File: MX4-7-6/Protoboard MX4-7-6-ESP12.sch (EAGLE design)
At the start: 294 parts

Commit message: Adjusted Polygon
Adjusted Polygon on all boxes. Changed length on MX-4-7-6 to fit the
box, it was 2mm to long.
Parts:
- removed PAD1, PAD119, PAD120, PAD121, PAD128, PAD129, PAD130, PAD137, PAD138, PAD139, PAD146, PAD147, PAD148, PAD151, PAD152, PAD153, PAD154, PAD155, PAD156, PAD157, PAD160, PAD161, PAD162, PAD163, PAD164, PAD165, PAD166, PAD2, PAD260, PAD261, PAD262, PAD263, PAD264, PAD265, PAD266, PAD273, PAD274, PAD275, PAD314, PAD315, PAD316, PAD317, PAD318, PAD319, PAD320, PAD332, PAD333, PAD334, PAD335, PAD336, PAD337, PAD338, PAD341, PAD342, PAD343, PAD344, PAD345, PAD346, PAD347, PAD350, PAD351, PAD352, PAD353, PAD354, PAD355, PAD356, PAD359, PAD360, PAD361, PAD362, PAD363, PAD364, PAD365, PAD368, PAD369, PAD370, PAD371, PAD372, PAD373, PAD374, PAD377, PAD378, PAD379, PAD380, PAD381, PAD382, PAD383, PAD385, PAD386, PAD387, PAD388, PAD389, PAD391, PAD392, PAD393, PAD394: (no value), wirepad:1,6/0,8
- removed X1: (no value), microbuilder:USBMICRO_20329
- added 5V, PAD104, PAD105, PAD113, PAD114, PAD3, PAD37, PAD41, PAD44, PAD48, PAD49, PAD50, PAD52, PAD53, PAD54, PAD56, PAD57, PAD58, PAD60, PAD61, PAD62, PAD64, PAD65, PAD66, PAD68, PAD69, PAD70, PAD71, PAD72, PAD73, PAD74, PAD76, PAD77, PAD78, PAD87, PAD96: (no value), wirepad:1,6/0,8
- added JP3: TX, adafruit:PINHD-1X1CB
- added JP4: RX, adafruit:PINHD-1X1CB
- added JP5: GND, adafruit:PINHD-1X1CB
- added MDL1: (no value), ESP8266-ESP12E:ESP8266-12EESP8266-ESP12E
- added MIC5502: (no value), SparkFun-PowerIC:MIC52053.3V
- added PAD47: AC, wirepad:1,6/0,8
- added PAD51: CH, wirepad:1,6/0,8
- added PAD55: 16, wirepad:1,6/0,8
- added PAD59: 14, wirepad:1,6/0,8
- added PAD63: 12, wirepad:1,6/0,8
- added PAD67: 13, wirepad:1,6/0,8
- added PAD75: CS, wirepad:1,6/0,8
- added PAD86: SI, wirepad:1,6/0,8
- added PAD95: RS, wirepad:1,6/0,8
- added X2: (no value), microbuilder:USBMICRO_20329
- PAD100: value (none) -> 5
- PAD103: value (none) -> SO
- PAD109: value (none) -> 4
- PAD111: value (none) -> 9
- PAD118: value (none) -> 0
- PAD127: value (none) -> 2
- PAD136: value (none) -> 15
- PAD145: value (none) -> SC
- PAD82: value (none) -> TX
- PAD91: value (none) -> RX
- PAD94: value (none) -> 10
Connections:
- removed net N$15: PAD151.P, PAD152.P, PAD153.P, PAD154.P, PAD155.P, PAD156.P, PAD157.P
- removed net N$16: PAD160.P, PAD161.P, PAD162.P, PAD163.P, PAD164.P, PAD165.P, PAD166.P
- removed net N$27: PAD260.P, PAD261.P, PAD262.P, PAD263.P, PAD264.P, PAD265.P, PAD266.P
- removed net N$3: PAD1.P, PAD2.P
- removed net N$33: PAD314.P, PAD315.P, PAD316.P, PAD317.P, PAD318.P, PAD319.P, PAD320.P
- removed net N$36: PAD341.P, PAD342.P, PAD343.P, PAD344.P, PAD345.P, PAD346.P, PAD347.P
- removed net N$37: PAD350.P, PAD351.P, PAD352.P, PAD353.P, PAD354.P, PAD355.P, PAD356.P
- removed net N$40: PAD377.P, PAD378.P, PAD379.P, PAD380.P, PAD381.P, PAD382.P, PAD383.P
- removed net N$41: PAD385.P, PAD386.P, PAD387.P, PAD388.P, PAD389.P
- removed net N$7: PAD79.P, PAD80.P, PAD81.P, PAD82.P, PAD83.P, PAD84.P, PAD85.P
- removed net N$8: PAD88.P, PAD89.P, PAD90.P, PAD91.P, PAD92.P, PAD93.P, PAD94.P
- new net N$26: MDL1.GPIO14, PAD59.P, PAD60.P, PAD61.P, PAD62.P
- new net N$42: MDL1.GPIO9, PAD111.P, PAD112.P, PAD113.P, PAD114.P
- new net N$50: MDL1.REST, PAD101.P, PAD102.P, PAD95.P, PAD96.P
- new net N$51: MDL1.ADC, PAD47.P, PAD48.P, PAD49.P, PAD50.P
- new net N$52: MDL1.CH_PD, PAD51.P, PAD52.P, PAD53.P, PAD54.P
- new net N$53: MDL1.GPIO16, PAD55.P, PAD56.P, PAD57.P, PAD58.P
- new net N$55: MDL1.GPIO12, PAD63.P, PAD64.P, PAD65.P, PAD66.P
- new net N$56: MDL1.GPIO13, PAD67.P, PAD68.P, PAD69.P, PAD70.P
- new net N$58: MDL1.MISO, PAD103.P, PAD104.P, PAD105.P, PAD110.P
- new net RX: JP4.1, MDL1.RXD, PAD88.P, PAD89.P, PAD90.P, PAD91.P
- new net TX: JP3.1, MDL1.TXD, PAD79.P, PAD80.P, PAD81.P, PAD82.P
- net GND: now also JP5.1, MDL1.GND, MIC5502.GND, X2.GND; no longer X1.GND
- net N$1: now also PAD3.P, PAD37.P, PAD41.P, PAD44.P; no longer PAD391.P, PAD392.P, PAD393.P, PAD394.P
- net N$10: now also MDL1.GPIO4; no longer PAD110.P, PAD111.P, PAD112.P
- net N$11: now also MDL1.GPIO0; no longer PAD119.P, PAD120.P, PAD121.P
- net N$12: now also MDL1.GPIO2; no longer PAD128.P, PAD129.P, PAD130.P
- net N$13: now also MDL1.GPIO15; no longer PAD137.P, PAD138.P, PAD139.P
- net N$14: now also MDL1.SCLK; no longer PAD146.P, PAD147.P, PAD148.P
- net N$28: no longer PAD273.P, PAD274.P, PAD275.P
- net N$29: now also PAD71.P
- net N$30: now also PAD72.P
- net N$31: now also PAD73.P
- net N$32: now also PAD74.P
- net N$35: now also MDL1.CS0, PAD75.P, PAD76.P, PAD77.P, PAD78.P; no longer PAD332.P, PAD333.P, PAD334.P, PAD335.P, PAD336.P, PAD337.P, PAD338.P
- net N$38: now also MDL1.MOSI, PAD83.P, PAD84.P, PAD85.P, PAD86.P; no longer PAD359.P, PAD360.P, PAD361.P, PAD362.P, PAD363.P, PAD364.P, PAD365.P
- net N$39: now also MDL1.GPIO10, PAD87.P, PAD92.P, PAD93.P, PAD94.P; no longer PAD368.P, PAD369.P, PAD370.P, PAD371.P, PAD372.P, PAD373.P, PAD374.P
- net N$9: now also MDL1.GPIO5; no longer PAD101.P, PAD102.P, PAD103.P
- net VCC: now also 5V.P, MIC5502.EN, MIC5502.IN, X2.VBUS; no longer X1.VBUS
- net VDD: now also MDL1.VCC, MIC5502.OUT

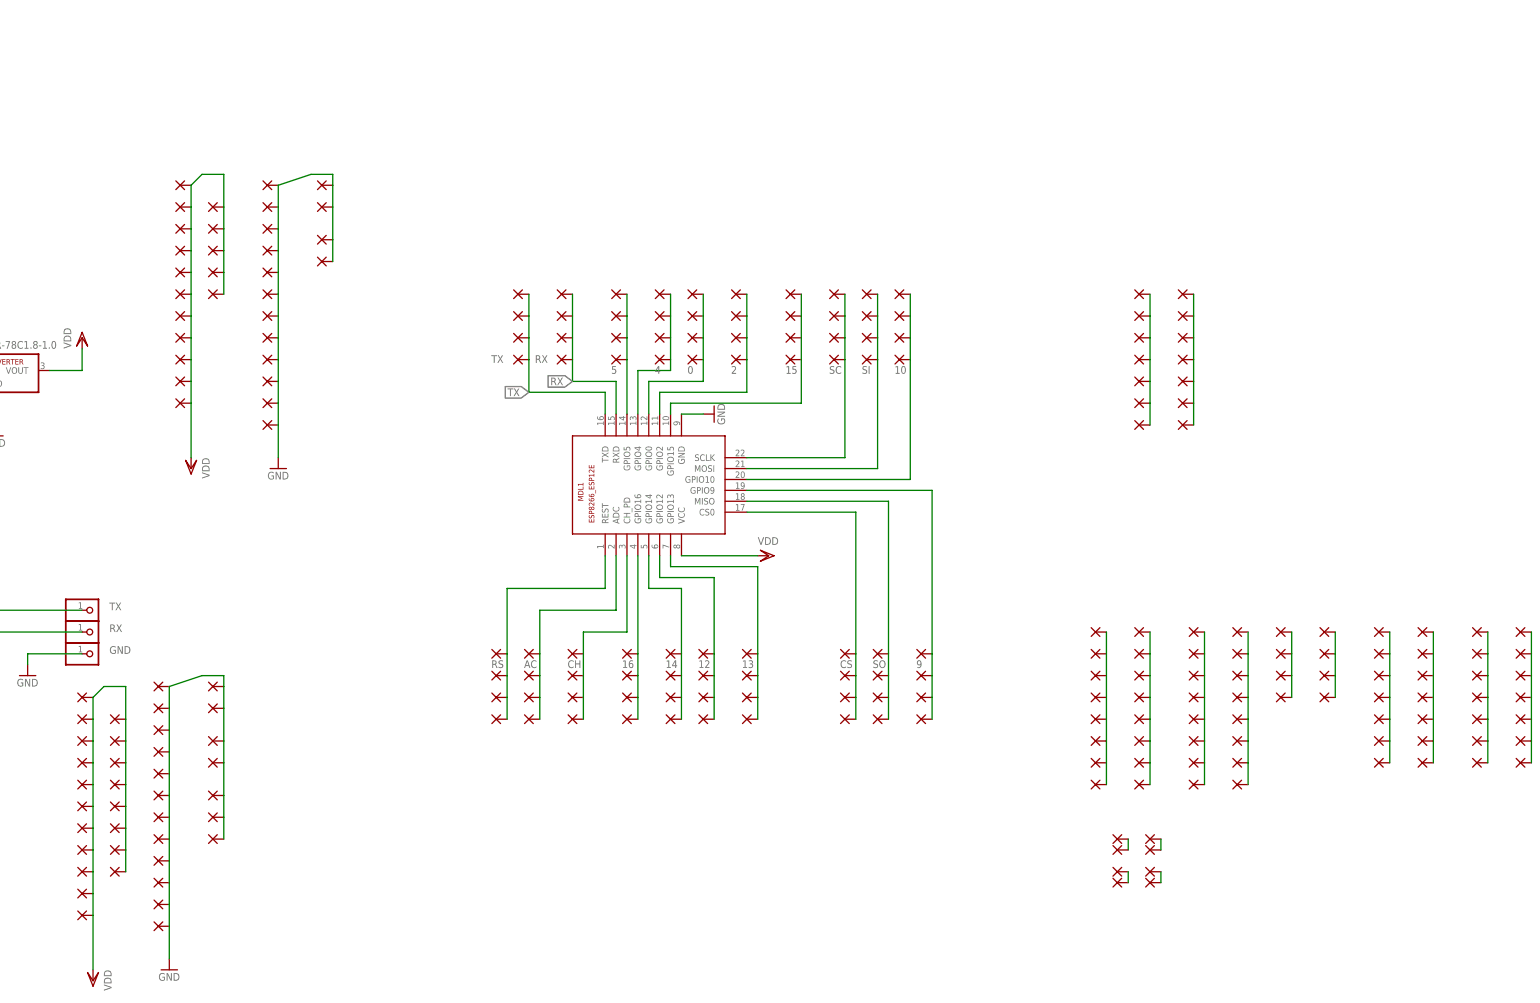
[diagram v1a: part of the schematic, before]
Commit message: Update to rev2
Updated to Pin headers instead of single wire pads
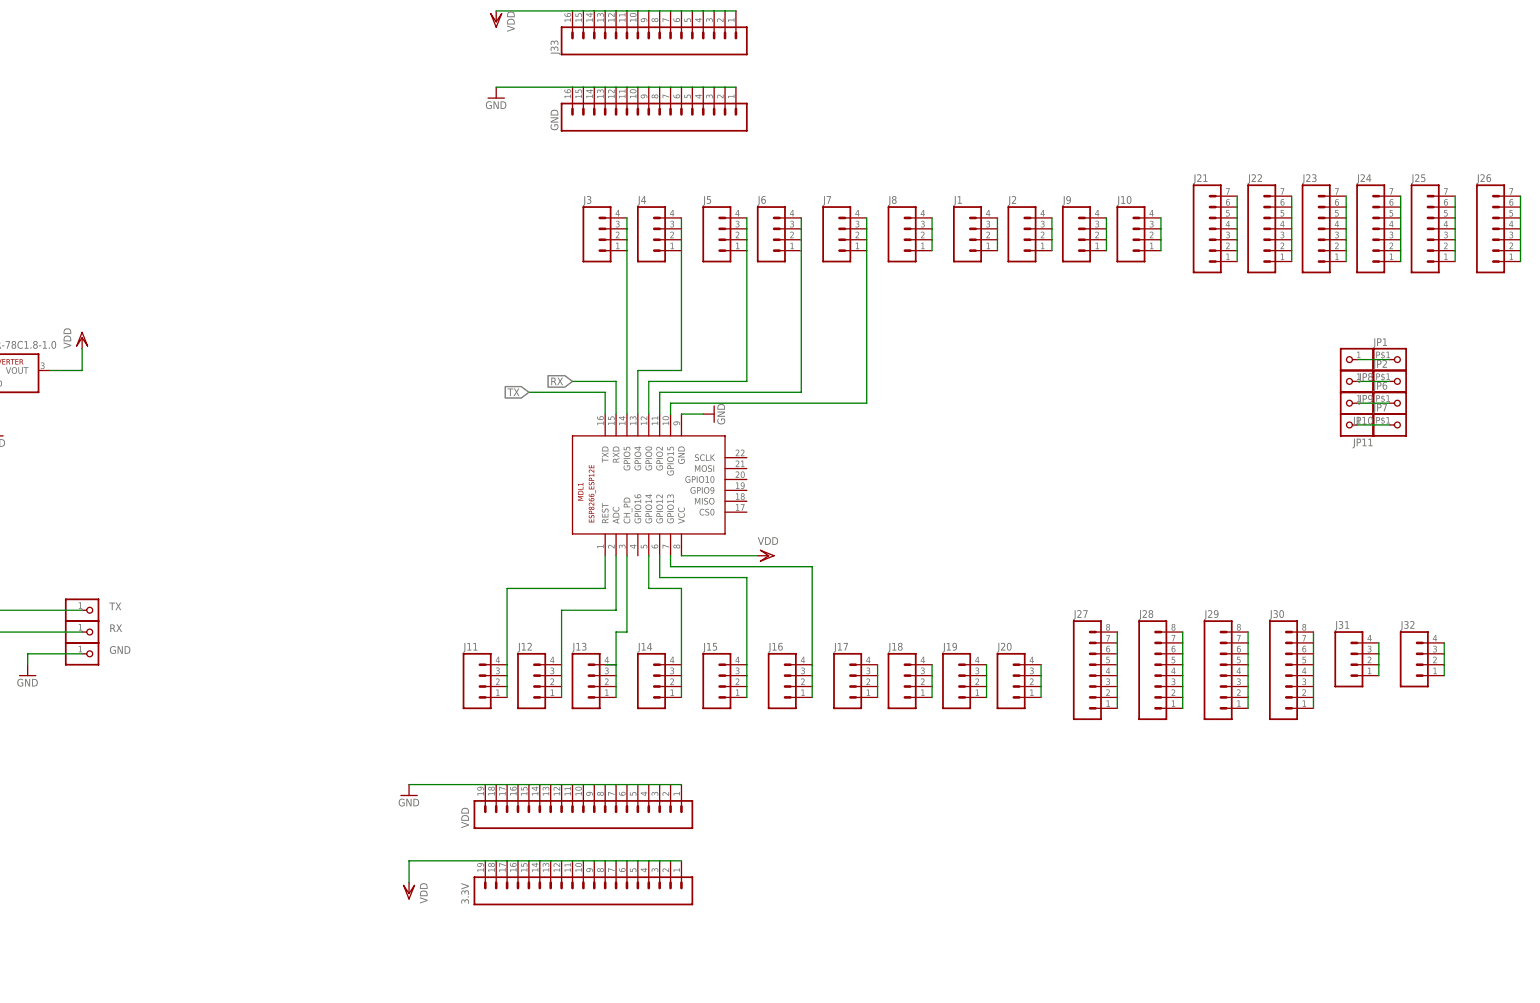
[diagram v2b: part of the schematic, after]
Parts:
- removed PAD10, PAD101, PAD102, PAD104, PAD105, PAD106, PAD107, PAD108, PAD11, PAD110, PAD112, PAD113, PAD114, PAD115, PAD116, PAD117, PAD12, PAD124, PAD125, PAD126, PAD13, PAD133, PAD134, PAD135, PAD14, PAD142, PAD143, PAD144, PAD15, PAD16, PAD169, PAD17, PAD170, PAD171, PAD172, PAD173, PAD174, PAD175, PAD178, PAD179, PAD18, PAD180, PAD181, PAD182, PAD183, PAD184, PAD187, PAD188, PAD189, PAD19, PAD190, PAD191, PAD192, PAD193, PAD196, PAD197, PAD198, PAD199, PAD20, PAD200, PAD201, PAD202, PAD205, PAD206, PAD207, PAD208, PAD209, PAD21, PAD210, PAD211, PAD214, PAD215, PAD216, PAD217, PAD218, PAD219, PAD22, PAD220, PAD23, PAD24, PAD25, PAD26, PAD269, PAD27, PAD270, PAD271, PAD272, PAD278, PAD279, PAD28, PAD280, PAD281, PAD282, PAD283, PAD284, PAD287, PAD288, PAD289, PAD29, PAD290, PAD291, PAD292, PAD293, PAD296, PAD297, PAD298, PAD299, PAD3, PAD30, PAD300, PAD301, PAD302, PAD305, PAD306, PAD307, PAD308, PAD309, PAD31, PAD310, PAD311, PAD32, PAD33, PAD36, PAD37, PAD38, PAD4, PAD41, PAD421, PAD422, PAD423, PAD424, PAD425, PAD426, PAD427, PAD428, PAD429, PAD430, PAD431, PAD432, PAD433, PAD434, PAD435, PAD436, PAD439, PAD44, PAD440, PAD441, PAD442, PAD443, PAD444, PAD445, PAD446, PAD447, PAD448, PAD449, PAD450, PAD451, PAD452, PAD453, PAD454, PAD455, PAD456, PAD459, PAD460, PAD461, PAD462, PAD48, PAD49, PAD5, PAD50, PAD52, PAD53, PAD54, PAD56, PAD57, PAD58, PAD6, PAD60, PAD61, PAD62, PAD64, PAD65, PAD66, PAD68, PAD69, PAD7, PAD70, PAD71, PAD72, PAD73, PAD74, PAD76, PAD77, PAD78, PAD79, PAD8, PAD80, PAD81, PAD83, PAD84, PAD85, PAD87, PAD88, PAD89, PAD9, PAD90, PAD92, PAD93, PAD96, PAD97, PAD98, PAD99: (no value), wirepad:1,6/0,8
- removed PAD100: 5, wirepad:1,6/0,8
- removed PAD103: SO, wirepad:1,6/0,8
- removed PAD109: 4, wirepad:1,6/0,8
- removed PAD111: 9, wirepad:1,6/0,8
- removed PAD118: 0, wirepad:1,6/0,8
- removed PAD127: 2, wirepad:1,6/0,8
- removed PAD136: 15, wirepad:1,6/0,8
- removed PAD145: SC, wirepad:1,6/0,8
- removed PAD34, PAD35, PAD39, PAD40, PAD42, PAD43, PAD45, PAD46: (no value), wirepad:3,17/1,3
- removed PAD47: AC, wirepad:1,6/0,8
- removed PAD51: CH, wirepad:1,6/0,8
- removed PAD55: 16, wirepad:1,6/0,8
- removed PAD59: 14, wirepad:1,6/0,8
- removed PAD63: 12, wirepad:1,6/0,8
- removed PAD67: 13, wirepad:1,6/0,8
- removed PAD75: CS, wirepad:1,6/0,8
- removed PAD82: TX, wirepad:1,6/0,8
- removed PAD86: SI, wirepad:1,6/0,8
- removed PAD91: RX, wirepad:1,6/0,8
- removed PAD94: 10, wirepad:1,6/0,8
- removed PAD95: RS, wirepad:1,6/0,8
- added 3.3V, VDD: (no value), SparkFun-Connectors:M191X19_NO_SILK
- added GND, J33: (no value), SparkFun-Connectors:M161X16_NO_SILK
- added J1, J10, J11, J12, J13, J14, J15, J16, J17, J18, J19, J2, J20, J3, J31, J32, J4, J5, J6, J7, J8, J9: (no value), SparkFun-Connectors:M04NO_SILK_ALL_ROUND
- added J21, J22, J23, J24, J25, J26: (no value), SparkFun-Connectors:M07NO_SILK
- added J27, J28, J29, J30: (no value), SparkFun-Connectors:M08NO_SILK_FEMALE_PTH
- added JP1, JP2, JP6, JP7: (no value), adafruit:PINHD-1X1-BIGPOGO
- added JP10, JP11, JP8, JP9: (no value), adafruit:PINHD-1X1CB
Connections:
- removed net N$2: PAD34.P, PAD35.P
- removed net N$38: MDL1.MOSI, PAD83.P, PAD84.P, PAD85.P, PAD86.P
- removed net N$39: MDL1.GPIO10, PAD87.P, PAD92.P, PAD93.P, PAD94.P
- removed net N$4: PAD39.P, PAD40.P
- removed net N$42: MDL1.GPIO9, PAD111.P, PAD112.P, PAD113.P, PAD114.P
- removed net N$5: PAD42.P, PAD43.P
- removed net N$53: MDL1.GPIO16, PAD55.P, PAD56.P, PAD57.P, PAD58.P
- removed net N$58: MDL1.MISO, PAD103.P, PAD104.P, PAD105.P, PAD110.P
- removed net N$6: PAD45.P, PAD46.P
- new net N$15: J10.1, J10.2, J10.3, J10.4
- new net N$16: J18.1, J18.2, J18.3, J18.4
- new net N$23: J19.1, J19.2, J19.3, J19.4
- new net N$24: J20.1, J20.2, J20.3, J20.4
- new net N$25: J28.1, J28.2, J28.3, J28.4, J28.5, J28.6, J28.7, J28.8
- new net N$27: J29.1, J29.2, J29.3, J29.4, J29.5, J29.6, J29.7, J29.8
- new net N$3: J8.1, J8.2, J8.3, J8.4
- new net N$33: JP10.1, JP6.1
- new net N$34: J17.1, J17.2, J17.3, J17.4
- new net N$7: J1.1, J1.2, J1.3, J1.4
- new net N$8: J2.1, J2.2, J2.3, J2.4
- net GND: now also GND.1, GND.10, GND.11, GND.12, GND.13, GND.14, GND.15, GND.16, GND.2, GND.3, GND.4, GND.5, GND.6, GND.7, GND.8, GND.9, VDD.1, VDD.10, VDD.11, VDD.12, VDD.13, VDD.14, VDD.15, VDD.16, VDD.17, VDD.18, VDD.19, VDD.2, VDD.3, VDD.4, VDD.5, VDD.6, VDD.7, VDD.8, VDD.9; no longer PAD17.P, PAD22.P, PAD23.P, PAD24.P, PAD25.P, PAD26.P, PAD27.P, PAD28.P, PAD29.P, PAD30.P, PAD31.P, PAD32.P, PAD33.P, PAD36.P, PAD38.P, PAD4.P, PAD421.P, PAD422.P, PAD423.P, PAD424.P, PAD425.P, PAD426.P, PAD427.P, PAD428.P, PAD429.P, PAD430.P, PAD431.P, PAD432.P, PAD433.P, PAD434.P, PAD435.P, PAD436.P, PAD439.P, PAD440.P, PAD441.P
- net N$1: now also J21.1, J21.2, J21.3, J21.4, J21.5, J21.6, J21.7; no longer PAD3.P, PAD37.P, PAD41.P, PAD44.P
- net N$10: now also J4.1, J4.2, J4.3, J4.4; no longer PAD106.P, PAD107.P, PAD108.P, PAD109.P
- net N$11: now also J5.1, J5.2, J5.3, J5.4; no longer PAD115.P, PAD116.P, PAD117.P, PAD118.P
- net N$12: now also J6.1, J6.2, J6.3, J6.4; no longer PAD124.P, PAD125.P, PAD126.P, PAD127.P
- net N$13: now also J7.1, J7.2, J7.3, J7.4; no longer PAD133.P, PAD134.P, PAD135.P, PAD136.P
- net N$14: now also J9.1, J9.2, J9.3, J9.4; no longer MDL1.SCLK, PAD142.P, PAD143.P, PAD144.P, PAD145.P
- net N$17: now also J22.1, J22.2, J22.3, J22.4, J22.5, J22.6, J22.7; no longer PAD169.P, PAD170.P, PAD171.P, PAD172.P, PAD173.P, PAD174.P, PAD175.P
- net N$18: now also J23.1, J23.2, J23.3, J23.4, J23.5, J23.6, J23.7; no longer PAD178.P, PAD179.P, PAD180.P, PAD181.P, PAD182.P, PAD183.P, PAD184.P
- net N$19: now also J24.1, J24.2, J24.3, J24.4, J24.5, J24.6, J24.7; no longer PAD187.P, PAD188.P, PAD189.P, PAD190.P, PAD191.P, PAD192.P, PAD193.P
- net N$20: now also J25.1, J25.2, J25.3, J25.4, J25.5, J25.6, J25.7; no longer PAD196.P, PAD197.P, PAD198.P, PAD199.P, PAD200.P, PAD201.P, PAD202.P
- net N$21: now also J26.1, J26.2, J26.3, J26.4, J26.5, J26.6, J26.7; no longer PAD205.P, PAD206.P, PAD207.P, PAD208.P, PAD209.P, PAD210.P, PAD211.P
- net N$22: now also J27.1, J27.2, J27.3, J27.4, J27.5, J27.6, J27.7, J27.8; no longer PAD214.P, PAD215.P, PAD216.P, PAD217.P, PAD218.P, PAD219.P, PAD220.P
- net N$26: now also J14.1, J14.2, J14.3, J14.4; no longer PAD59.P, PAD60.P, PAD61.P, PAD62.P
- net N$28: now also J30.1, J30.2, J30.3, J30.4, J30.5, J30.6, J30.7, J30.8; no longer PAD269.P, PAD270.P, PAD271.P, PAD272.P
- net N$29: now also J31.1, J31.2, J31.3, J31.4; no longer PAD278.P, PAD279.P, PAD280.P, PAD281.P, PAD282.P, PAD283.P, PAD284.P, PAD71.P
- net N$30: now also J32.1, J32.2, J32.3, J32.4; no longer PAD287.P, PAD288.P, PAD289.P, PAD290.P, PAD291.P, PAD292.P, PAD293.P, PAD72.P
- net N$31: now also JP1.1, JP8.1; no longer PAD296.P, PAD297.P, PAD298.P, PAD299.P, PAD300.P, PAD301.P, PAD302.P, PAD73.P
- net N$32: now also JP2.1, JP9.1; no longer PAD305.P, PAD306.P, PAD307.P, PAD308.P, PAD309.P, PAD310.P, PAD311.P, PAD74.P
- net N$35: now also JP11.1, JP7.1; no longer MDL1.CS0, PAD75.P, PAD76.P, PAD77.P, PAD78.P
- net N$50: now also J11.1, J11.2, J11.3, J11.4; no longer PAD101.P, PAD102.P, PAD95.P, PAD96.P
- net N$51: now also J12.1, J12.2, J12.3, J12.4; no longer PAD47.P, PAD48.P, PAD49.P, PAD50.P
- net N$52: now also J13.1, J13.2, J13.3, J13.4; no longer PAD51.P, PAD52.P, PAD53.P, PAD54.P
- net N$55: now also J15.1, J15.2, J15.3, J15.4; no longer PAD63.P, PAD64.P, PAD65.P, PAD66.P
- net N$56: now also J16.1, J16.2, J16.3, J16.4; no longer PAD67.P, PAD68.P, PAD69.P, PAD70.P
- net N$9: now also J3.1, J3.2, J3.3, J3.4; no longer PAD100.P, PAD97.P, PAD98.P, PAD99.P
- net RX: no longer PAD88.P, PAD89.P, PAD90.P, PAD91.P
- net TX: no longer PAD79.P, PAD80.P, PAD81.P, PAD82.P
- net VDD: now also 3.3V.1, 3.3V.10, 3.3V.11, 3.3V.12, 3.3V.13, 3.3V.14, 3.3V.15, 3.3V.16, 3.3V.17, 3.3V.18, 3.3V.19, 3.3V.2, 3.3V.3, 3.3V.4, 3.3V.5, 3.3V.6, 3.3V.7, 3.3V.8, 3.3V.9, J33.1, J33.10, J33.11, J33.12, J33.13, J33.14, J33.15, J33.16, J33.2, J33.3, J33.4, J33.5, J33.6, J33.7, J33.8, J33.9; no longer PAD10.P, PAD11.P, PAD12.P, PAD13.P, PAD14.P, PAD15.P, PAD16.P, PAD18.P, PAD19.P, PAD20.P, PAD21.P, PAD442.P, PAD443.P, PAD444.P, PAD445.P, PAD446.P, PAD447.P, PAD448.P, PAD449.P, PAD450.P, PAD451.P, PAD452.P, PAD453.P, PAD454.P, PAD455.P, PAD456.P, PAD459.P, PAD460.P, PAD461.P, PAD462.P, PAD5.P, PAD6.P, PAD7.P, PAD8.P, PAD9.P

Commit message: Update esp component and usb
test
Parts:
- removed MDL1: (no value), ESP8266-ESP12E:ESP8266-12EESP8266-ESP12E
- added X1: ESP-12E, microbuilder:ESP-12E
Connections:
- net GND: now also X1.GND; no longer MDL1.GND
- net N$10: now also X1.GPIO4; no longer MDL1.GPIO4
- net N$11: now also X1.GPIO0; no longer MDL1.GPIO0
- net N$12: now also X1.GPIO2; no longer MDL1.GPIO2
- net N$13: now also X1.GPIO15; no longer MDL1.GPIO15
- net N$26: now also X1.GPIO16; no longer MDL1.GPIO14
- net N$34: now also X1.GPIO13
- net N$50: now also X1.RESET; no longer MDL1.REST
- net N$51: now also X1.ADC; no longer MDL1.ADC
- net N$52: now also X1.CH_PD; no longer MDL1.CH_PD
- net N$55: now also X1.GPIO14; no longer MDL1.GPIO12
- net N$56: now also X1.GPIO12; no longer MDL1.GPIO13
- net N$9: now also X1.GPIO5; no longer MDL1.GPIO5
- net RX: now also X1.RXD; no longer MDL1.RXD
- net TX: now also X1.TXD; no longer MDL1.TXD
- net VDD: now also X1.VCC; no longer MDL1.VCC

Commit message: Routing and Gerber files
Routed and produced gerber files
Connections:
- removed net N$3: J8.1, J8.2, J8.3, J8.4
- removed net N$7: J1.1, J1.2, J1.3, J1.4
- net RX: now also J1.1, J1.2, J1.3, J1.4
- net TX: now also J8.1, J8.2, J8.3, J8.4
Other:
- moved on the sheet: J1, J8
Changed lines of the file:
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@@
 <instance part="J6" gate="G$1" x="154.94" y="93.98"/>
 <instance part="J7" gate="G$1" x="170.18" y="93.98"/>
-<instance part="J8" gate="G$1" x="185.42" y="93.98"/>
-<instance part="J1" gate="G$1" x="200.66" y="93.98"/>
+<instance part="J8" gate="G$1" x="86.36" y="93.98"/>
+<instance part="J1" gate="G$1" x="101.6" y="93.98"/>
 <instance part="J2" gate="G$1" x="213.36" y="93.98"/>
 <instance part="J9" gate="G$1" x="226.06" y="93.98"/>
@@
 <pinref part="X1" gate="G$1" pin="TXD"/>
 <junction x="114.3" y="55.88"/>
+<wire x1="96.52" y1="58.42" x2="96.52" y2="83.82" width="0.1524" layer="91"/>
+<pinref part="J8" gate="G$1" pin="1"/>
+<pinref part="J8" gate="G$1" pin="2"/>
+<wire x1="91.44" y1="91.44" x2="91.44" y2="93.98" width="0.1524" layer="91"/>
+<pinref part="J8" gate="G$1" pin="3"/>
+<wire x1="91.44" y1="93.98" x2="91.44" y2="96.52" width="0.1524" layer="91"/>
+<pinref part="J8" gate="G$1" pin="4"/>
+<wire x1="91.44" y1="96.52" x2="91.44" y2="99.06" width="0.1524" layer="91"/>
+<wire x1="96.52" y1="83.82" x2="91.44" y2="83.82" width="0.1524" layer="91"/>
+<wire x1="91.44" y1="83.82" x2="91.44" y2="91.44" width="0.1524" layer="91"/>
 </segment>
 <segment>
@@
 <pinref part="X1" gate="G$1" pin="RXD"/>
 <junction x="116.84" y="55.88"/>
+<pinref part="J1" gate="G$1" pin="4"/>
+<pinref part="J1" gate="G$1" pin="3"/>
+<wire x1="106.68" y1="99.06" x2="106.68" y2="96.52" width="0.1524" layer="91"/>
+<pinref part="J1" gate="G$1" pin="2"/>
+<wire x1="106.68" y1="96.52" x2="106.68" y2="93.98" width="0.1524" layer="91"/>
+<pinref part="J1" gate="G$1" pin="1"/>
+<wire x1="106.68" y1="93.98" x2="106.68" y2="91.44" width="0.1524" layer="91"/>
+<wire x1="106.68" y1="60.96" x2="106.68" y2="91.44" width="0.1524" layer="91"/>
 </segment>
 <segment>
@@
 </segment>
 </net>
-<net name="N$3" class="0">
-<segment>
-<pinref part="J8" gate="G$1" pin="1"/>
-<pinref part="J8" gate="G$1" pin="2"/>
-<wire x1="190.5" y1="91.44" x2="190.5" y2="93.98" width="0.1524" layer="91"/>
-<pinref part="J8" gate="G$1" pin="3"/>
-<wire x1="190.5" y1="93.98" x2="190.5" y2="96.52" width="0.1524" layer="91"/>
-<pinref part="J8" gate="G$1" pin="4"/>
-<wire x1="190.5" y1="96.52" x2="190.5" y2="99.06" width="0.1524" layer="91"/>
-</segment>
-</net>
-<net name="N$7" class="0">
-<segment>
-<pinref part="J1" gate="G$1" pin="4"/>
-<pinref part="J1" gate="G$1" pin="3"/>
-<wire x1="205.74" y1="99.06" x2="205.74" y2="96.52" width="0.1524" layer="91"/>
-<pinref part="J1" gate="G$1" pin="2"/>
-<wire x1="205.74" y1="96.52" x2="205.74" y2="93.98" width="0.1524" layer="91"/>
-<pinref part="J1" gate="G$1" pin="1"/>
-<wire x1="205.74" y1="93.98" x2="205.74" y2="91.44" width="0.1524" layer="91"/>
-</segment>
-</net>
